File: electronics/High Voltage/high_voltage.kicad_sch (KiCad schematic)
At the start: 48 parts, among them J1 EG HV, J2 FILAMENT, J3 BIAS, Y1 DC 24V, Y2 DC 24V

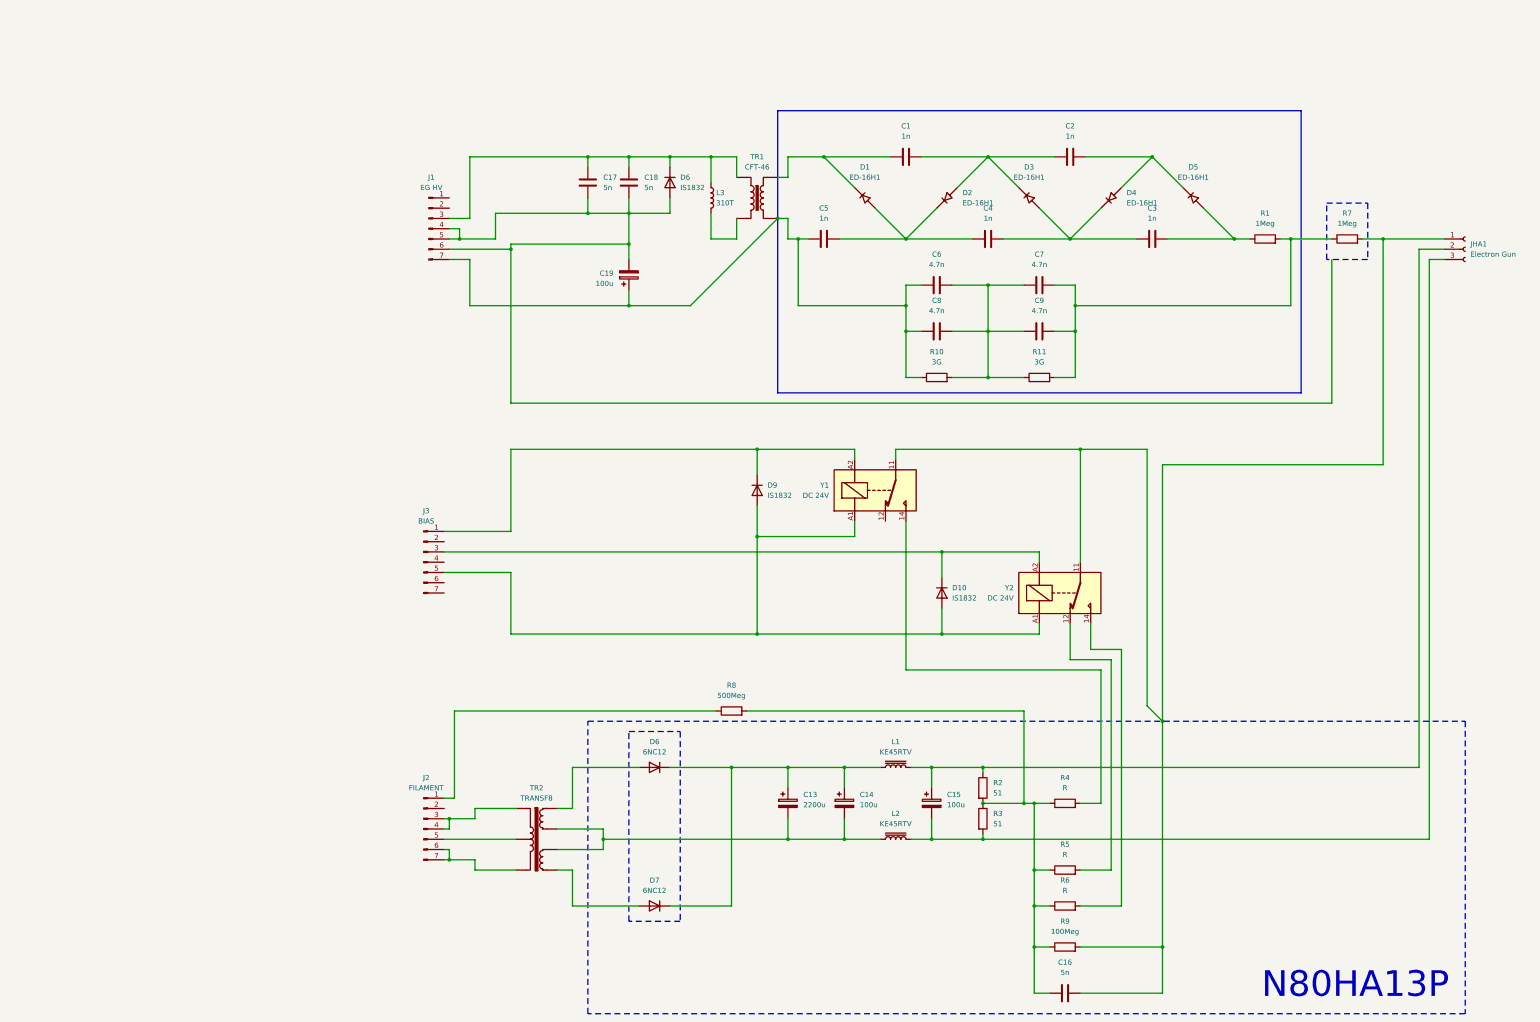
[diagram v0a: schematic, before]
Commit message: Added Dry HV electron gun circuit
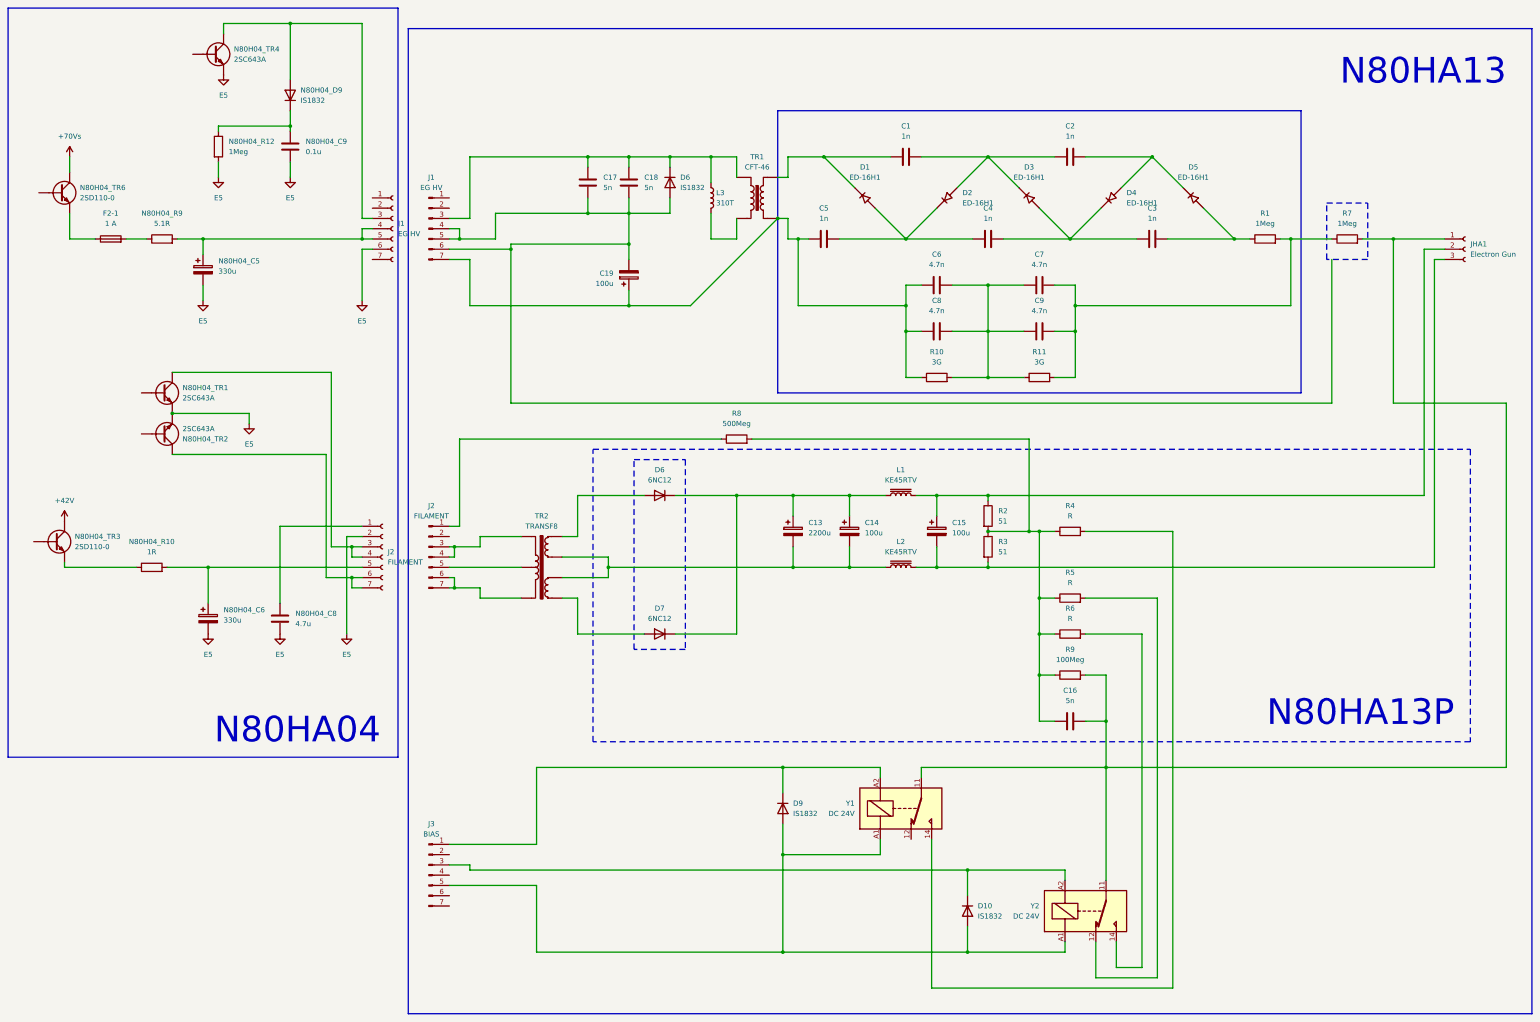
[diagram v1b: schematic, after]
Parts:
- added F2-1: 1 A, symbol Device:Fuse
- added J1: EG HV, symbol Connector:Conn_01x07_Socket
- added J2: FILAMENT, symbol Connector:Conn_01x07_Socket
- added N80H04_C5, N80H04_C6: 330u, symbol Device:C_Polarized
- added N80H04_C8: 4.7u, symbol Device:C
- added N80H04_C9: 0.1u, symbol Device:C
- added N80H04_D9: IS1832, symbol Device:D
- added N80H04_R10: 1R, symbol Device:R
- added N80H04_R12: 1Meg, symbol Device:R
- added N80H04_R9: 5.1R, symbol Device:R
- added N80H04_TR1, N80H04_TR2, N80H04_TR4: 2SC643A, symbol Device:Q_NPN
- added N80H04_TR3, N80H04_TR6: 2SD110-0, symbol Device:Q_NPN
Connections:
- new net: J2.1 (Pin_1), N80H04_C8.1
- new net: J2.3 (Pin_3), J2.4 (Pin_4), N80H04_TR1.C
- new net: J2.5 (Pin_5), N80H04_C6.1, N80H04_R10.2
- new net: J2.6 (Pin_6), J2.7 (Pin_7), N80H04_TR2.C
- new net: N80H04_C9.1, N80H04_D9.1 (K), N80H04_R12.1
- new net: J1.3 (Pin_3), N80H04_D9.2 (A), N80H04_TR4.C
- new net: J1.4 (Pin_4), J1.5 (Pin_5), N80H04_C5.1, N80H04_R9.2
- new net: F2-1.1, N80H04_TR6.E
- new net: F2-1.2, N80H04_R9.1
- new net: N80H04_R10.1, N80H04_TR3.E
- new net +42V: N80H04_TR3.C
- new net +70Vs: N80H04_TR6.C
- new net E5: J1.6 (Pin_6), J2.2 (Pin_2), N80H04_C5.2, N80H04_C6.2, N80H04_C8.2, N80H04_C9.2, N80H04_R12.2, N80H04_TR1.E, N80H04_TR2.E, N80H04_TR4.E
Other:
- note added: "N80HA04"
- note added: "N80HA13"
- moved on the sheet: C13, C14, C15, C16, D10, D6, D7, D9, J2, J3, L1, L2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

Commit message: Completed EG parts of N80H04
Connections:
- net PINT: now reaches J2.1 (Pin_1), N80H04_C8.1
- net PIN16: now reaches F2-1.1, N80H04_TR6.E
- net PIN4-D: now reaches N80H04_TR2.B
- net PIN10-L: now reaches N80H04_TR4.B
- net PIN2-B: now reaches N80H04_TR1.B
- net PIN20-X: now reaches N80H04_TR6.B
- net PINH: now reaches N80H04_R10.1, N80H04_TR3.E
- net EC_OUT: now reaches J1.7 (Pin_7)
- net PIN7: now reaches N80H04_TR3.B
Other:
- note added: "N80HA04 (partial)"
- note removed: "N80HA04"
- moved on the sheet: N80H04_C6, N80H04_C8, N80H04_C9, N80H04_D9, N80H04_R10, N80H04_R12, N80H04_TR1, N80H04_TR2, N80H04_TR3, N80H04_TR4, N80H04_TR6

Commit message: Added N80HC01 to High Voltage
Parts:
- added N80HC01_C1: 220u, symbol Device:C_Polarized
- added N80HC01_C10, N80HC01_C13, N80HC01_C2, N80HC01_C29, N80HC01_C30, N80HC01_C31: 100u, symbol Device:C_Polarized
- added N80HC01_C11, N80HC01_C12, N80HC01_C21: 0.1u, symbol Device:C
- added N80HC01_C14, N80HC01_C15, N80HC01_C16, N80HC01_C17, N80HC01_C6, N80HC01_C7: 1n, symbol Device:C
- added N80HC01_C18: 3.6n, symbol Device:C
- added N80HC01_C19, N80HC01_C25, N80HC01_C27, N80HC01_C5: 220p, symbol Device:C
- added N80HC01_C23, N80HC01_C8: 47u, symbol Device:C_Polarized
- added N80HC01_C26: 4.7n, symbol Device:C
- added N80HC01_C28: 47n, symbol Device:C
- added N80HC01_C3: 100p, symbol Device:C
- added N80HC01_C4: 68n, symbol Device:C
- added N80HC01_CP1: FILAMENT 8kHz, symbol Connector:TestPoint
- added N80HC01_CP2: FILAMENT DRIVE, symbol Connector:TestPoint
- added N80HC01_CP3: FIL. VOL., symbol Connector:TestPoint
- added N80HC01_CP4: OSC, symbol Connector:TestPoint
- added N80HC01_CP5: EG HV DRIVE, symbol Connector:TestPoint
- added N80HC01_CP6: EG HV VOLTAGE, symbol Connector:TestPoint
- added N80HC01_D1, N80HC01_D2, N80HC01_D4: IS1587, symbol Device:D
- added N80HC01_IC1, N80HC01_IC3, N80HC01_IC4: ${SIM.PARAMS}, symbol Simulation_SPICE:OPAMP
- added N80HC01_IC2, UN80HC01_IC2: LM741, symbol Amplifier_Operational:LM741
- added N80HC01_L1, N80HC01_L2, N80HC01_L3: 33u, symbol Device:L_Iron
- added N80HC01_R1, N80HC01_R13, N80HC01_R31, N80HC01_R43, N80HC01_R52, N80HC01_R53, N80HC01_R54: 10, symbol Device:R
- added N80HC01_R1, N80HC01_R26, N80HC01_R35: 51k, symbol Device:R
- added N80HC01_R10, N80HC01_R11, N80HC01_R21, N80HC01_R23, N80HC01_R24, N80HC01_R28, N80HC01_R29, N80HC01_R36, N80HC01_R49, N80HC01_R6, N80HC01_R9: 10k, symbol Device:R
- added N80HC01_R12, N80HC01_R30, N80HC01_R39, N80HC01_R44, N80HC01_R50, N80HC01_R7: 1k, symbol Device:R
- added N80HC01_R14, N80HC01_R15 (x2), N80HC01_R34, N80HC01_R5: 2k, symbol Device:R
- added N80HC01_R16: 510, symbol Device:R
- added N80HC01_R16, N80HC01_R2, N80HC01_R4, N80HC01_R41, N80HC01_R42: 5.1k, symbol Device:R
- added N80HC01_R17: 34k, symbol Device:R
- added N80HC01_R18: 3.9k, symbol Device:R
- added N80HC01_R19: 2.7k, symbol Device:R
- added N80HC01_R2, N80HC01_R20, N80HC01_R3: 200, symbol Device:R
- added N80HC01_R27, N80HC01_R8, N80M01_R17: 100k, symbol Device:R
- added N80HC01_R32: 150k, symbol Device:R
- added N80HC01_R33: 7.5k, symbol Device:R
- added N80HC01_R38: 20Meg, symbol Device:R
- added N80HC01_R48: 100, symbol Device:R
- added N80HC01_RV1, N80HC01_RV2, N80HC01_RV3: 10k, symbol Device:R_Potentiometer_Trim
- added N80HC01_T1: 32T:6T-6T, symbol Transformer:TRANSF4
- added N80HC01_TR2, N80HC01_TR3, N80HC01_TR5: 2SC484-Y, symbol Device:Q_NPN
- added N80HC01_ZD1: RD6A-M, symbol Device:D_Zener
- added N80HC01_ZD11, N80HC01_ZD12, N80HC01_ZD4, N80HC01_ZD7: RD19A, symbol Device:D_Zener
- added N80HC01_ZD2, N80HC01_ZD3, N80HC01_ZD5, N80HC01_ZD6: RD6A, symbol Device:D_Zener
- added N80M01_M1: 300uA Full Scale, symbol Device:Ammeter_DC
- added N80M01_S4: VAC./EMIS./W.D.F., symbol Switch:SW_DP3T
- added Q1, Q4, Q6: Q_NPN, symbol Device:Q_NPN
- added TR4: TRANSF4, symbol Transformer:TRANSF4
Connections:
- net +42V: now also N80HC01_R15.1, N80HC01_TR2.C
- net +70Vs: now also N80HC01_R42.1, Q6.C
- net E5: now also N80HC01_T1.2, N80M01_R17.2, N80M01_S4.6, TR4.3
- net EC_OUT: now also N80M01_R17.1, N80M01_S4.2
- net PIN10-L: now also N80HC01_C31.2, N80HC01_R53.1
- net PIN16: now also N80HC01_CP6.1, N80HC01_R38.1
- net PIN2-B: now also N80HC01_C29.2, N80HC01_R31.1
- net PIN20-X: now also Q6.E
- net PIN4-D: now also N80HC01_C30.2, N80HC01_R52.1
- net PIN7: now also N80HC01_TR2.E
- net PINH: now also N80HC01_C10.1, N80HC01_CP3.1, N80HC01_R17.2
- net PINT: now also N80HC01_C21.1, N80HC01_R35.1, N80HC01_R36.2
- net at C17.2, C18.2, C19.2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: no longer J1.4 (Pin_4), J1.5 (Pin_5)
- net at L3.2, TR1.2: now also J1.4 (Pin_4), J1.5 (Pin_5)
- new net: N80HC01_R5.2, N80HC01_R6.1, Q1.B
- new net: N80HC01_C28.1, N80HC01_CP2.1, N80HC01_T1.5, Q1.C
- new net: N80HC01_ZD2.1 (K), N80HC01_ZD3.1 (K)
- new net: N80HC01_C18.1, N80HC01_IC4.2 (-), N80HC01_R29.1, N80HC01_ZD2.2 (A)
- new net: N80HC01_C11.1, N80HC01_R18.2, N80HC01_R19.2, N80HC01_ZD1.1 (K)
- new net: N80HC01_R39.1, N80HC01_TR5.B
- new net: N80HC01_R41.1, N80HC01_TR5.C, Q6.B
- new net: N80HC01_IC3.1 (+), N80HC01_R21.2, N80HC01_R26.1
- new net: N80HC01_IC3.2 (-), N80HC01_R24.2
- new net: N80HC01_CP4.1, N80HC01_IC3.5, N80HC01_R11.2, N80HC01_R23.2, N80HC01_R30.1, N80HC01_R44.1
- new net: N80HC01_R32.1, N80HC01_R33.1, N80HC01_R34.1, N80HC01_RV3.1
- new net: N80HC01_R15.1, N80HC01_R32.2
- new net: N80HC01_C23.1, N80HC01_R41.2, N80HC01_R42.2
- new net: N80HC01_C27.1, N80HC01_C3.1, N80HC01_CP1.1, N80HC01_IC1.5, N80HC01_R50.2, N80HC01_R6.2, N80HC01_R7.1, N80HC01_R8.2
- new net: N80HC01_D4.1 (K), N80HC01_IC1.1 (+), N80HC01_R8.1, N80HC01_R9.2
- new net: N80HC01_C4.1, N80HC01_D1.1 (K), N80HC01_IC1.2 (-), N80HC01_RV1.2, N80HC01_RV1.3
- new net: N80HC01_L1.1, N80HC01_R2.2, N80HC01_T1.1
- new net: N80HC01_L2.1, N80HC01_R3.2, N80HC01_T1.3
- new net: N80HC01_C2.1, N80HC01_C28.2, N80HC01_R4.1, N80HC01_T1.4
- new net: N80HC01_C5.1, N80HC01_R11.1
- new net: N80HC01_C5.2, N80HC01_D2.2 (A), N80HC01_R10.2
- new net: N80HC01_C30.1, N80HC01_L2.2, N80HC01_R3.1, N80HC01_R52.2
- new net: N80HC01_R23.1, Q4.B
- new net: N80HC01_C26.1, N80HC01_CP5.1, Q4.C, TR4.5
- new net: N80HC01_R7.2, N80HC01_RV1.1
- new net: N80HC01_C29.1, N80HC01_L1.2, N80HC01_R2.1, N80HC01_R31.2
- new net: N80HC01_C31.1, N80HC01_L3.2, N80HC01_R20.1, N80HC01_R54.2
- new net: N80HC01_L3.1, N80HC01_R20.2, TR4.1
- new net: N80HC01_C8.1, N80HC01_R12.2, N80HC01_TR3.B
- new net: N80HC01_C8.2, N80HC01_R13.2
- new net: N80HC01_IC4.1 (+), N80HC01_R27.1, N80HC01_R28.2
- new net: N80HC01_IC4.5, N80HC01_R26.2, N80HC01_R27.2, N80HC01_RV2.1, N80HC01_RV2.2
- new net: N80HC01_C1.1, N80HC01_R1.1, N80HC01_R35.2
- new net: N80HC01_R1.2, N80HC01_RV3.2
- new net: N80HC01_R53.2, N80HC01_R54.1
- new net: N80HC01_R29.2, N80HC01_RV2.3
- new net: N80HC01_R39.2, UN80HC01_IC2.6
- new net: N80HC01_R36.1, N80HC01_ZD5.1 (K), UN80HC01_IC2.2 (-)
- new net: N80HC01_R2.2, N80HC01_R38.2, UN80HC01_IC2.3 (+)
- new net: N80HC01_D2.1 (K), N80HC01_D4.2 (A), N80HC01_R49.2
- new net: N80HC01_ZD5.2 (A), N80HC01_ZD6.2 (A)
- new net: N80HC01_R16.1, N80HC01_R33.2
- new net: N80HC01_IC2.3 (+), N80HC01_R16.1, N80HC01_R17.1
- new net: N80M01_M1.1 (-), N80M01_S4.7
- new net: N80HC01_C13.1, N80HC01_R48.1, TR4.4
- new net: N80HC01_IC2.6, N80HC01_R12.1
- new net: N80M01_M1.2 (+), N80M01_S4.3
- new net: N80HC01_R14.1, N80HC01_R15.2
- new net: N80HC01_R14.2, N80HC01_TR2.B, N80HC01_TR3.C
- new net: N80HC01_C26.2, N80HC01_R48.2
- new net +15V: N80HC01_R1.1, N80HC01_R18.1, N80HC01_ZD11.1 (K)
- new net +15Vso: N80HC01_C14.1, N80HC01_C16.2, N80HC01_C6.1, N80HC01_IC1.3 (V+), N80HC01_IC2.7 (V+), N80HC01_IC3.3 (V+), N80HC01_IC4.3 (V+), N80HC01_R1.2, N80HC01_R4.2, N80HC01_ZD7.1 (K), UN80HC01_IC2.7 (V+)
- new net -15V: N80HC01_R43.1, N80HC01_ZD12.2 (A)
- new net -15Vso: N80HC01_C15.1, N80HC01_C17.1, N80HC01_C7.1, N80HC01_IC1.4 (V-), N80HC01_IC2.4 (V-), N80HC01_IC3.4 (V-), N80HC01_IC4.4 (V-), N80HC01_R43.2, N80HC01_ZD4.2 (A), UN80HC01_IC2.4 (V-)
- new net GND1: N80HC01_C2.2, N80HC01_C27.2, N80HC01_C3.2, N80HC01_C4.2, N80HC01_C6.2, N80HC01_C7.2, N80HC01_D1.2 (A), N80HC01_R10.1, N80HC01_R49.1, N80HC01_R5.1, N80HC01_R9.1, Q1.E
- new net GND2: N80HC01_C10.2, N80HC01_C11.2, N80HC01_C12.1, N80HC01_R13.1, N80HC01_R16.2, N80HC01_TR3.E, N80HC01_ZD1.2 (A)
- new net GND3: N80HC01_C13.2, N80HC01_C14.2, N80HC01_C15.2, N80HC01_C16.1, N80HC01_C17.2, N80HC01_C18.2, N80HC01_C19.2, N80HC01_C25.2, N80HC01_R21.1, N80HC01_R24.1, N80HC01_R28.1, N80HC01_ZD3.2 (A), N80HC01_ZD4.1 (K), N80HC01_ZD7.2 (A), Q4.E
- new net GND4: N80HC01_C1.2, N80HC01_C21.2, N80HC01_C23.2, N80HC01_R2.1, N80HC01_RV3.3, N80HC01_TR5.E, N80HC01_ZD11.2 (A), N80HC01_ZD12.1 (K), N80HC01_ZD6.1 (K)
- new net PIN11-M: N80HC01_R50.1
- new net PIN14-R: N80HC01_C19.1, N80HC01_R44.2
- new net PIN15-S: N80HC01_C25.1, N80HC01_R30.2
- new net PIN18: N80HC01_R16.2
- new net PIN9: N80HC01_C12.2, N80HC01_IC2.2 (-)
- new net PINK: N80HC01_R19.1
- new net PINU: N80HC01_R15.2
- new net PINV: N80HC01_R34.2
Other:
- note added: "HIGH"
- note added: "LOW"
- note added: "MEDIUM"
- note added: "N80HC01"
- note added: "N80M01 (partial)"
- note added: "VOL. Negative Feedback (NF)"
- moved on the sheet: C1, C13, C14, C15, C16, C17, C18, C19, C2, C3, C4, C5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

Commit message: Added all circuits to the High Voltage schematic
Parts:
- added J4: Conn_01x07_Socket, symbol Connector:Conn_01x07_Socket
- added N80HC01_R22: 200, symbol Device:R
- added N80HC01_R31: 1k, symbol Device:R
- added N80HC01_ZD4: IS2192, symbol Device:D_Zener
- added N80M01_RV8: 5k, symbol Device:R_Potentiometer
- added N80M01_S1, N80M01_S6: H.V. Select, symbol Switch:SW_Rotary_1x5_MP
- renumbered UN80HC01_IC2 to N80HC01_IC5
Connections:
- net +15Vso: now also N80HC01_R22.1, N80HC01_R31.2
- net GND2: now also N80HC01_C12.2; no longer N80HC01_C12.1
- net GND4: now also N80HC01_ZD4.2 (A)
- net at N80HC01_C13.1, N80HC01_R48.1, TR4.4: now also N80HC01_R22.2
- net PIN18 renamed JH1_L
- net PIN9 renamed JH1_H
- net JH1_H: now also N80HC01_C12.1; no longer N80HC01_C12.2
- net PINK renamed JH1_G
- net PINU renamed JH1_K
- net PINV renamed JH1_M
- new net +24V: N80M01_S1.6
- new net E23: J4.5 (Pin_5)
- new net JH1_J: N80HC01_R31.1, N80HC01_ZD4.1 (K)
- new net JM4_X: N80M01_RV8.1
- new net JM4_Y: N80M01_RV8.2
- new net JM4_Z: N80M01_RV8.3
- new net JM4_a: N80M01_S6.6
- new net JM4_b: N80M01_S6.1, N80M01_S6.2
- new net JM4_c: N80M01_S6.3, N80M01_S6.4
- new net JM4_d: N80M01_S6.5
- new net JM4_g: J4.1 (Pin_1), N80M01_S1.1, N80M01_S1.2
- new net JM4_h: J4.3 (Pin_3), N80M01_S1.3, N80M01_S1.4
- new net JM4_j: N80M01_S1.5
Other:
- note added: "COMMON"
- note added: "Electron Gun Voltage Drive"
- note added: "Electron Gun Voltage Feedback"
- note added: "Filament Drive"
- note added: "N80M01"
- note added: "Oscillator"
- note added: "Reference for Emission Control"
- note added: "Reference for High Voltage Selector"
- note added: "Right-side Front Panel"
- note added: "Triangle to square(?) wave"
- note added: "Unused"
- note added: "Voltage Negative Feedback (VOL NF)"
- note removed: "VOL. Negative Feedback (NF)"
- moved on the sheet: C1, C13, C14, C15, C16, C17, C18, C19, C2, C3, C4, C5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

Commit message: EG filament and notes added
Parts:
- added J5: Conn_01x03_Pin, symbol Connector:Conn_01x03_Pin
- added L4: L, symbol Device:L
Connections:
- new net: J5.2 (Pin_2), L4.1
- new net: J5.3 (Pin_3), L4.2
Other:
- note added: "Electron Gun"
- note added: "N80HA04"
- note added: "N80M01 User Controls"
- note added: "N80M01 read-out"
- note removed: "N80HA04 (partial)"
- note removed: "N80M01"
- note removed: "N80M01 (partial)"
